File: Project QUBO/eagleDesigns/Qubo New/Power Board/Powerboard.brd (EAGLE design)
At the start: 100 x 80 mm, 45 parts, among them IC1 PCF8574T, U1 UEI15

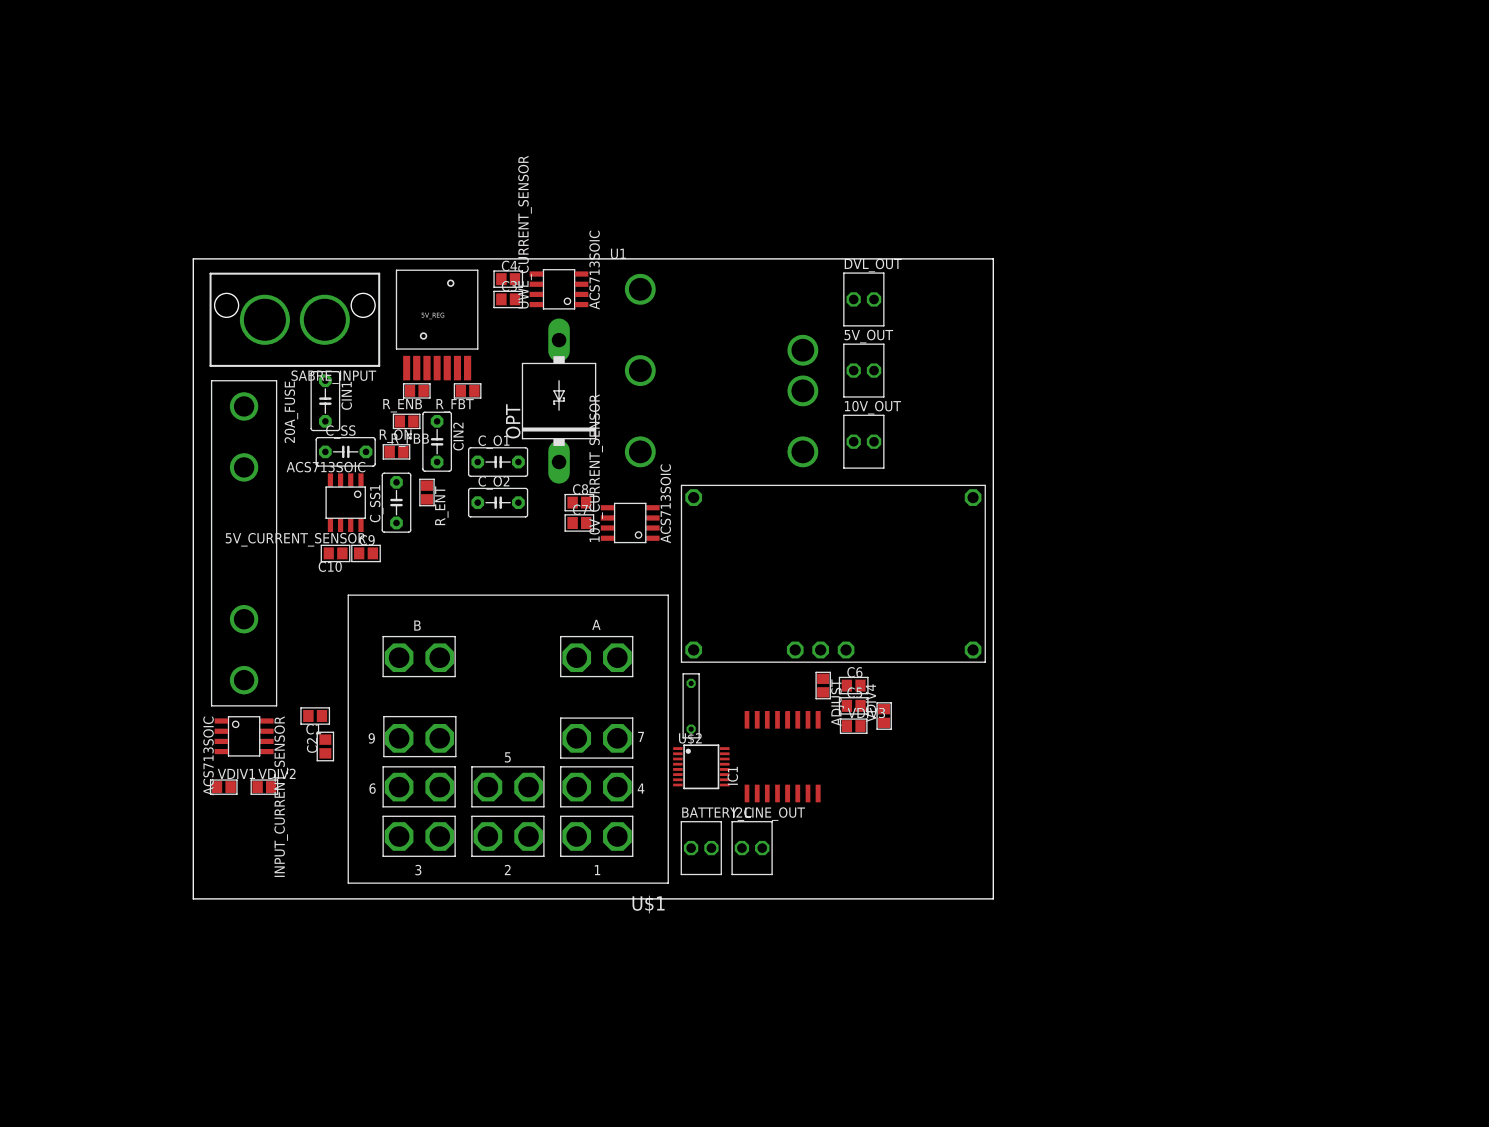
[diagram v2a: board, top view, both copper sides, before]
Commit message: 
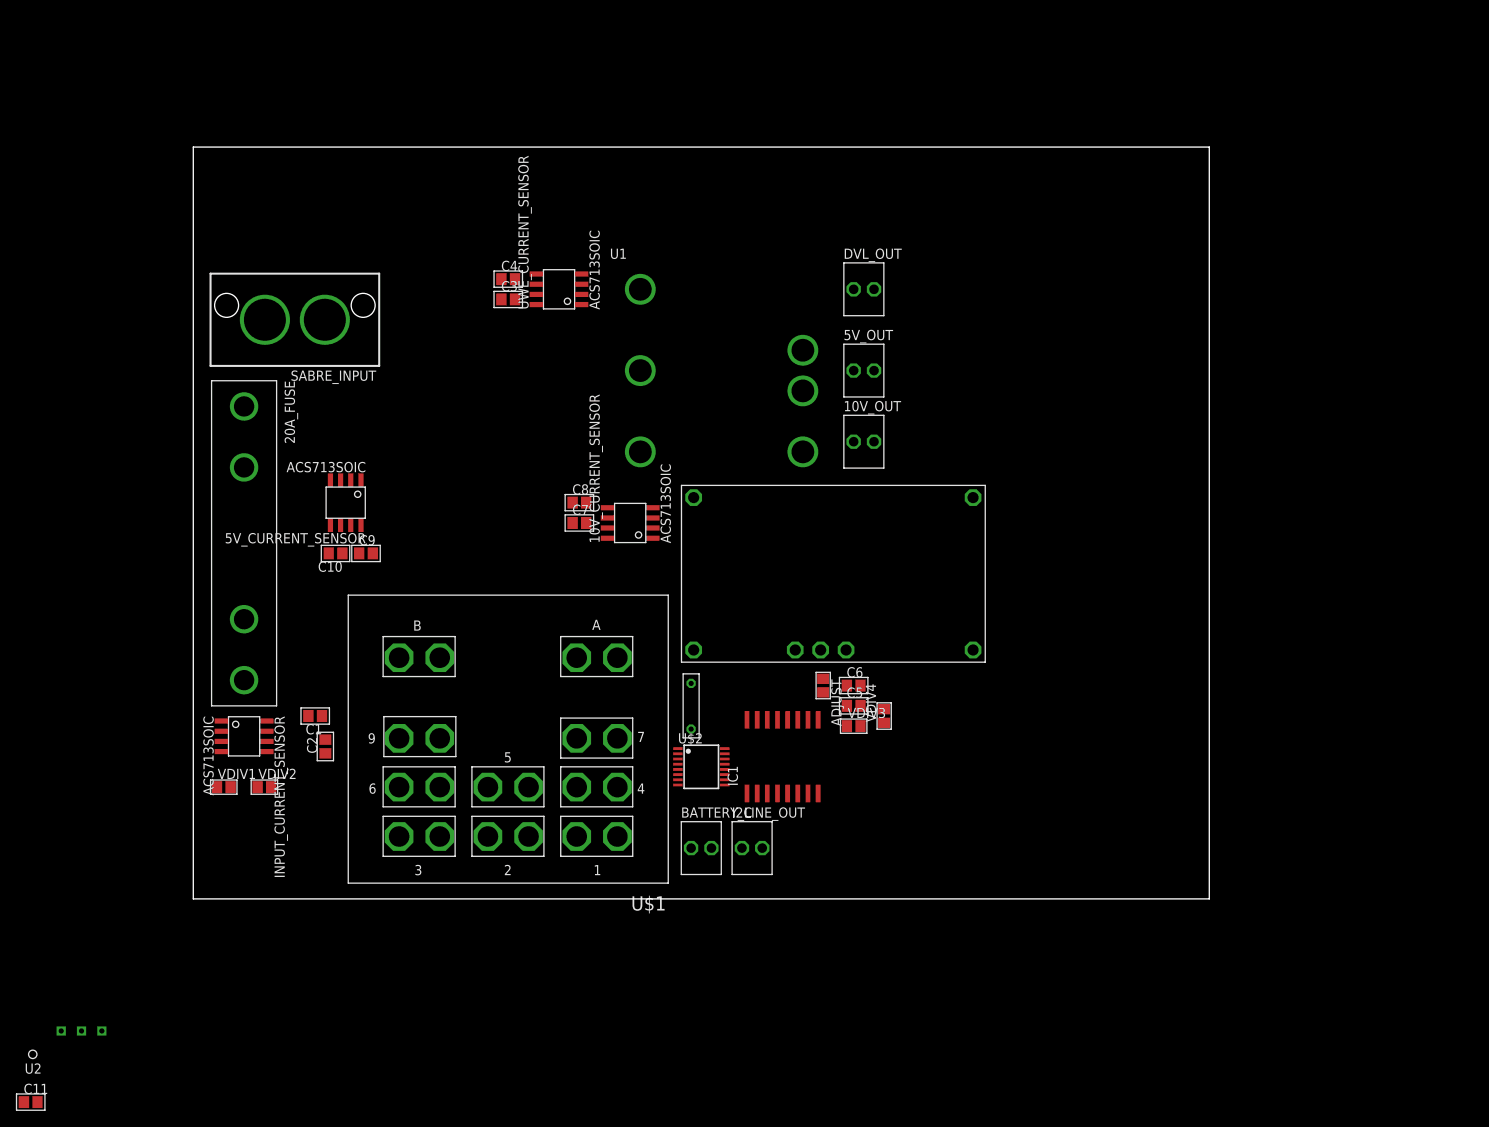
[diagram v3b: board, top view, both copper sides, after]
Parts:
- removed 5V_REG: LMZ120017-PIN, texas:LMZ12001
- removed CIN1, CIN2, C_O1, C_O2, C_SS, C_SS1: (no value), capacitor-wima:C5B3.5
- removed OPT: BZW50, diode:AG
- removed R_ENB, R_ENT, R_FBB, R_FBT, R_ON: (no value), resistor:R0805
- added C11: FILTER, resistor:C0805
- added U2: TSR2-2450, tracoPower:TSR2
- moved DVL_OUT 1.27 mm to (83.8, 76.2)
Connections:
- removed net N$12: 5V_REG.2, R_ON.1
- removed net N$13: 5V_REG.5, C_SS.2
- removed net N$15: 5V_REG.7, C_O1.2, C_O2.2, C_SS1.1, R_FBT.1
- removed net N$16: 5V_REG.3, OPT.C, R_ENB.1, R_ENT.1
- removed net N$17: 5V_REG.6, C_SS1.2, R_FBB.2, R_FBT.2
- new net N$4: 5V_CURRENT_SENSOR.P$1, 5V_CURRENT_SENSOR.P$2, 5V_CURRENT_SENSOR.P$8, C11.1, C9.2, U2.3
- net 5V_EN: no longer R_ENT.2
- net GND: now also C11.2, U2.2
- net PROCESSED_INPUT: now also U2.1; no longer 5V_CURRENT_SENSOR.P$1, 5V_CURRENT_SENSOR.P$2, 5V_CURRENT_SENSOR.P$8, 5V_REG.1, 5V_REG.4, C9.2, CIN1.1, CIN1.2, CIN2.1, CIN2.2, C_O1.1, C_O2.1, C_SS.1, OPT.A, R_ENB.2, R_FBB.1, R_ON.2
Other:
- board size 100 x 80 mm -> 127 x 94 mm

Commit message: Power board changes
worked on layout and routing of power board
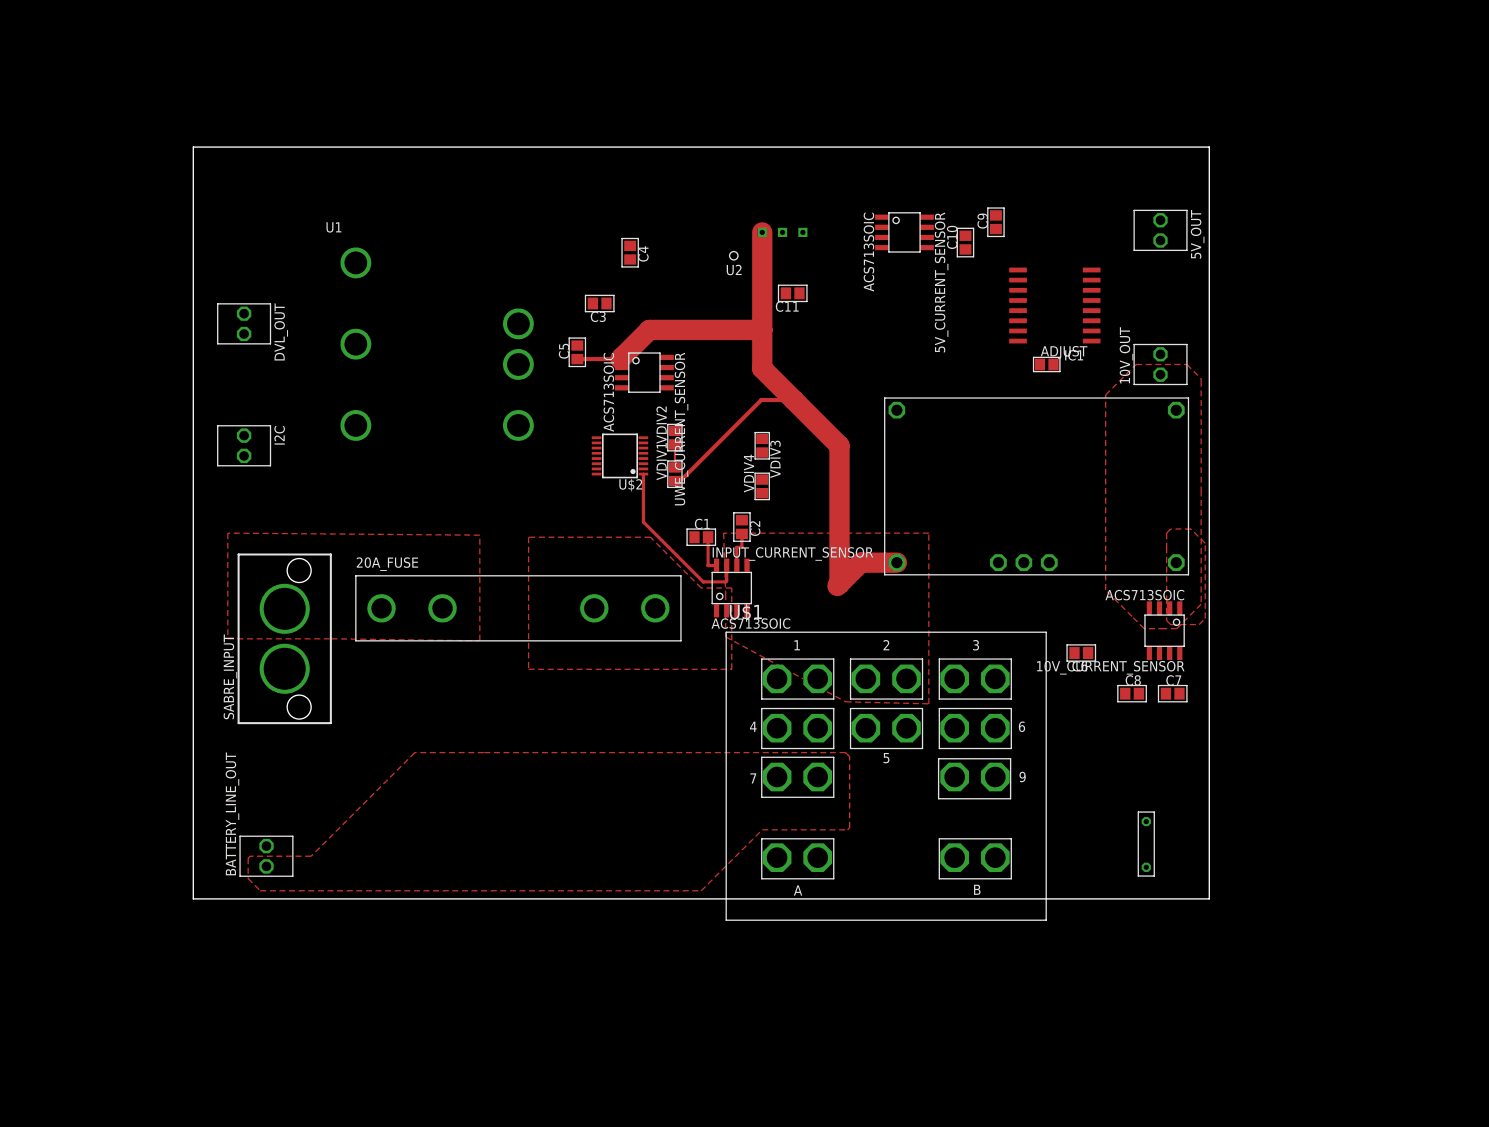
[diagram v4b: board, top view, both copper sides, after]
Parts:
- moved C11 138.9 mm to (74.9, 75.7), turned to 180 degrees
- moved U2 132.8 mm to (73.7, 83.3)
- moved C9 89.0 mm to (100.3, 84.6), turned to 90 degrees
- moved C10 87.8 mm to (96.5, 82.0), turned to 90 degrees
- moved I2C 81.0 mm to (6.35, 56.6), turned to 270 degrees
- moved 5V_CURRENT_SENSOR 77.6 mm to (88.9, 83.3), turned to 270 degrees
- moved DVL_OUT 77.6 mm to (6.35, 71.9), turned to 270 degrees
- moved C7 77.2 mm to (122.4, 25.7)
- moved C8 73.1 mm to (117.3, 25.7)
- moved VDIV1 68.6 mm to (60.2, 53.1), turned to 90 degrees
- moved 10V_CURRENT_SENSOR 68.1 mm to (121.4, 33.5), turned to 180 degrees
- moved VDIV2 67.4 mm to (60.2, 57.7), turned to 90 degrees
- moved IC1 65.9 mm to (107.7, 74.2), turned to 90 degrees
- moved INPUT_CURRENT_SENSOR 63.7 mm to (67.3, 38.9), turned to 0 degrees
- moved MAGREAD 59.5 mm to (119.1, 6.86)
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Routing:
- net PROCESSED_INPUT: track 0.00 -> 99.8 mm
- net INPUT_CURRENT: track 0.00 -> 21.6 mm
- net 5V: track 0.00 -> 4.61 mm
- net N$2: track 0.00 -> 4.61 mm
- net INPUT_VOLTAGE: track 0.00 -> 2.87 mm
- added copper zone on layer 1, net 10V_OUT
- added copper zone on layer 1, net BATTERY_LINE
- added copper zone on layer 1, net N$1
- added copper zone on layer 1, net PROCESSED_10V_OUT
- added copper zone on layer 1, net PROCESSED_INPUT
- added copper zone on layer 1, net VBAT

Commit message: PowerBoard update
Updated powerboard wiring, and resized.
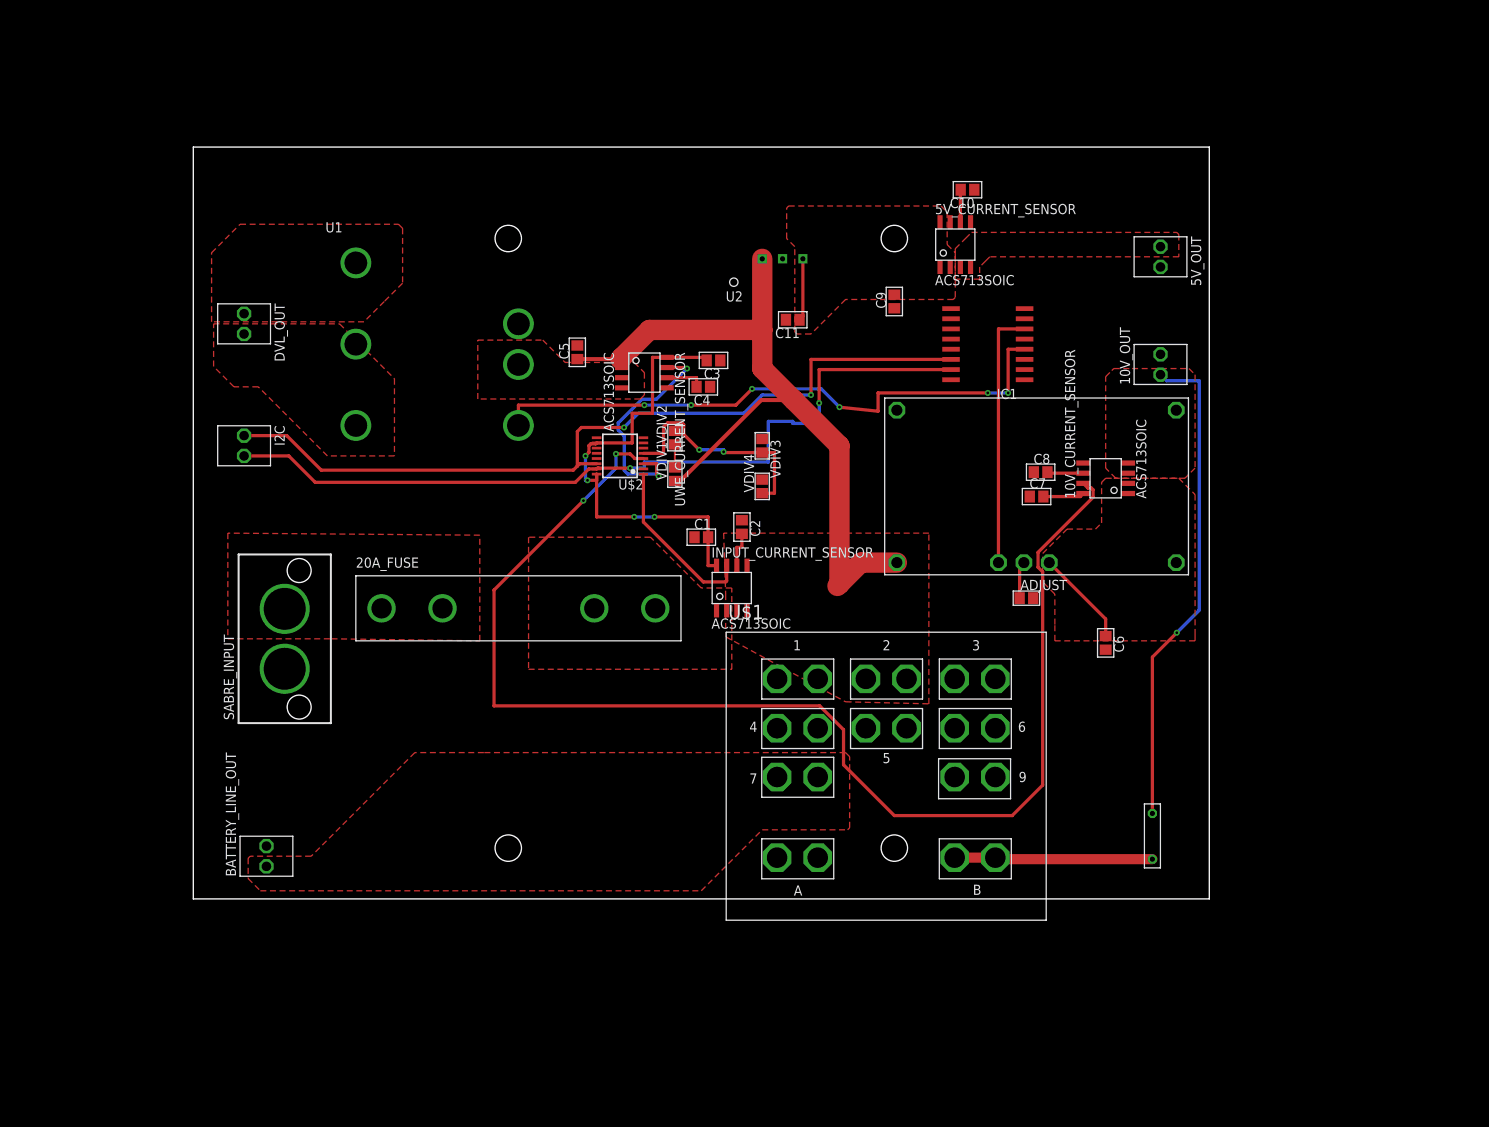
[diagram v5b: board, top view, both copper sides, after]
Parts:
- moved C8 30.0 mm to (105.9, 53.3)
- moved C7 29.9 mm to (105.4, 50.3)
- moved ADJUST 29.3 mm to (104.1, 37.6)
- moved 10V_CURRENT_SENSOR 20.4 mm to (114.0, 52.6), turned to 90 degrees
- moved C4 19.1 mm to (63.8, 64.0), turned to 180 degrees
- moved C9 16.1 mm to (87.6, 74.7)
- moved C3 15.9 mm to (65.0, 67.3)
- moved IC1 9.67 mm to (99.3, 69.3)
- moved C10 6.61 mm to (96.8, 88.6), turned to 180 degrees
- moved 5V_CURRENT_SENSOR 6.53 mm to (95.2, 81.8), turned to 0 degrees
- moved 5V_OUT 3.30 mm to (120.9, 80.3)
- moved C6 3.30 mm to (114.0, 32.0), turned to 270 degrees
- moved C11 3.30 mm to (74.9, 72.4)
- moved U2 3.30 mm to (73.7, 80.0)
- moved MAGREAD 1.27 mm to (119.9, 7.87)
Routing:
- net 10V_CURRENT: track 0.00 -> 161.5 mm, vias 0 -> 2
- net SCL: track 0.00 -> 103.6 mm, vias 0 -> 2
- net SDA: track 0.00 -> 103.3 mm, vias 0 -> 2
- net UEI_EN: track 0.00 -> 75.4 mm, vias 0 -> 6
- net PROCESSED_10V_OUT: track 0.00 -> 61.6 mm, vias 0 -> 1
- net 5V: track 4.61 -> 64.2 mm, vias 0 -> 4
- net 10V_EN: track 0.00 -> 32.5 mm
- net 10V_VOLTAGE: track 0.00 -> 29.0 mm, vias 0 -> 2
- net UWE_CURRENT: track 0.00 -> 28.1 mm, vias 0 -> 2
- net N$9: track 0.00 -> 24.8 mm
- net 10V_OUT: track 0.00 -> 12.1 mm
- net N$4: track 0.00 -> 7.79 mm
- net N$5: track 0.00 -> 4.98 mm
- net N$7: track 0.00 -> 4.86 mm
- net N$10: track 0.00 -> 4.53 mm
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- added copper zone on layer 1, net 5V
- added copper zone on layer 1, net N$4
- added copper zone on layer 1, net PROCESSED_UEI_OUTPUT
- added copper zone on layer 1, net UEI_GND
- added copper zone on layer 1, net UEI_INPUT

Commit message: 
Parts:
- moved C10 8.20 mm to (104.6, 86.4)
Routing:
- net 5V: track 64.2 -> 165.0 mm, vias 4 -> 6
- net GND: track 0.00 -> 89.9 mm, vias 0 -> 16
- net 5V_CURRENT: track 0.00 -> 67.7 mm, vias 0 -> 2
- net PROCESSED_10V_OUT: track 61.6 -> 116.5 mm, vias 1 -> 2
- net INPUT_VOLTAGE: track 2.87 -> 11.5 mm
- net SDA: track 103.3 -> 95.6 mm
- net N$3: track 4.07 -> 9.61 mm
- net 10V_VOLTAGE: track 29.0 -> 33.6 mm
- net PROCESSED_INPUT: track 96.5 -> 98.7 mm
- added copper zone on layer 16, net GND
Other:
- board size 127 x 94 mm -> 127 x 88.9 mm

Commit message: Finished PowerboardRev1
Revision 1 of the Powerboard
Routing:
- net PROCESSED_10V_OUT: vias 2 -> 4
